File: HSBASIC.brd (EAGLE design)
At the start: 44 x 44 mm, 25 parts, among them IC1 ESP12SMT, IC3 MS563702BA03, IC4 DHT12

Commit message: Routing
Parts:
- removed R3: 10K, freetronics-jon:0603
- moved R10 1.50 mm to (26.0, 40.5), turned to 180 degrees
- moved R7 1.50 mm to (26.0, 40.5), turned to 0 degrees
- turned LED2 to 0 degrees
- turned LED3 to 180 degrees
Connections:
- removed net N$11: LED3.A, R7.1
- new net N$5: LED2.C, R10.2
- net 3.3V: now also LED2.A, LED3.A; no longer R3.2
- net GND: no longer LED2.C, LED3.C
- net GPIO16: no longer R10.2, R7.2
- net GPIO2: now also R10.1, R7.1; no longer R3.1
- net N$4: now also LED3.C, R7.2; no longer LED2.A, R10.1
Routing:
- net GPIO2: track 17.0 -> 33.8 mm, vias 0 -> 2
- net GPIO16: track 13.6 -> 0.00 mm, vias 1 -> 0
- net 3.3V: track 110.5 -> 123.5 mm, vias 2 -> 3
- net N$11: track 3.98 -> 0.00 mm
- net N$5: track 0.00 -> 2.48 mm
- net N$4: track 3.98 -> 2.48 mm
- net GND: track 27.9 -> 28.9 mm
- net TXD: track 45.0 -> 44.4 mm
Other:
- outline, holes or cut-outs redrawn

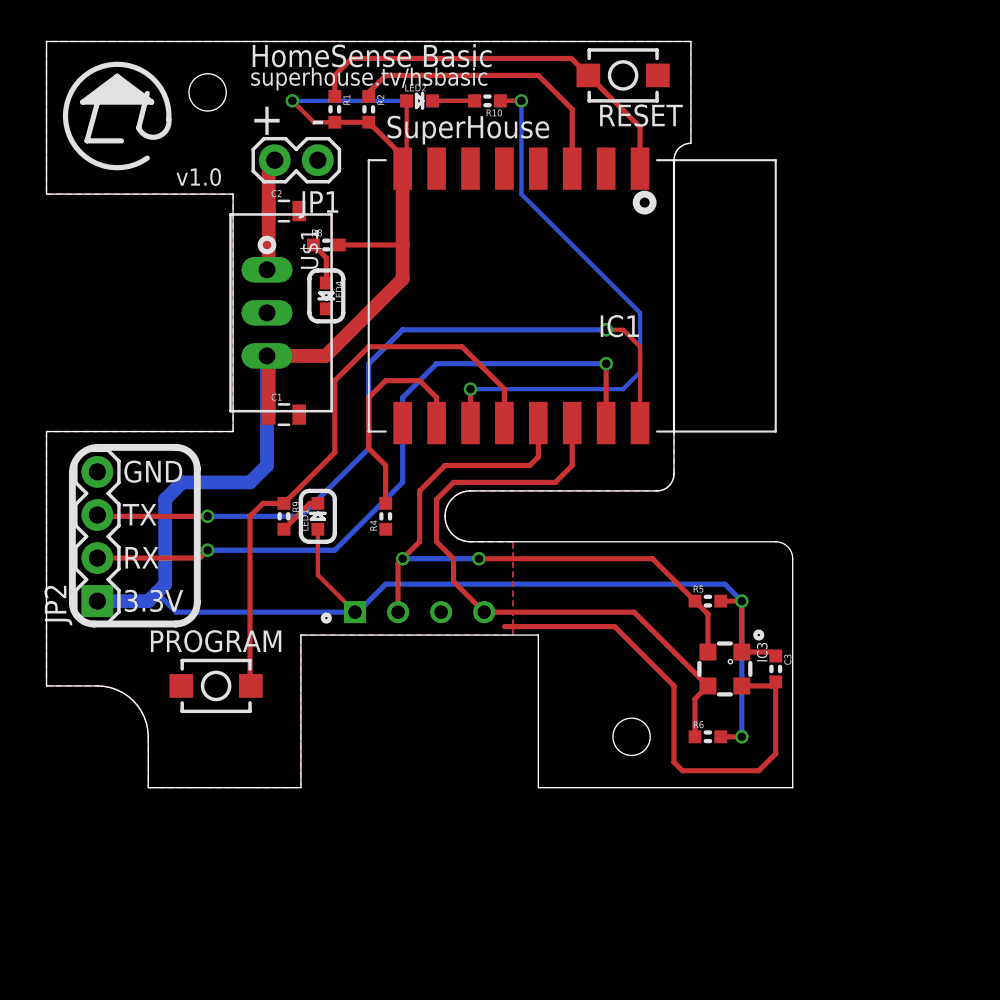
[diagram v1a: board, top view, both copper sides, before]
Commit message: Switch to BME280 sensor for Tasmota compatibility
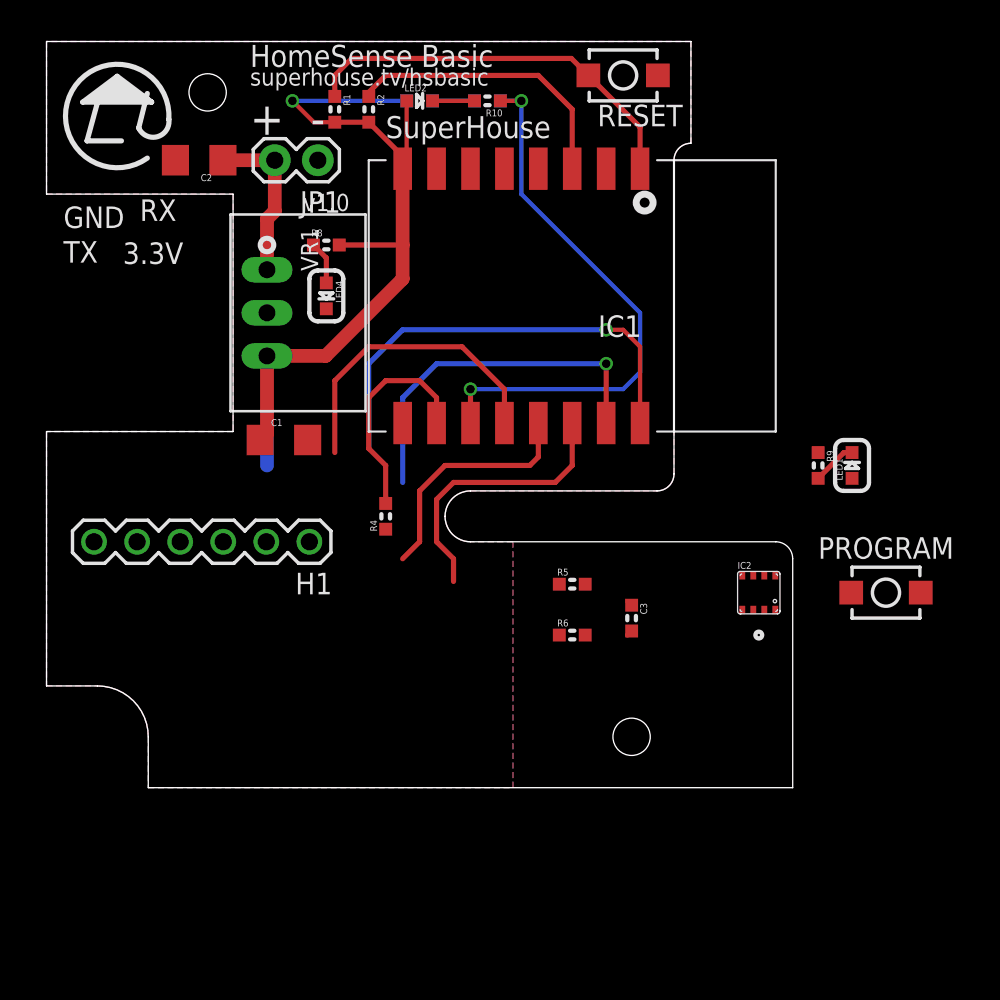
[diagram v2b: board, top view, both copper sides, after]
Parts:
- removed IC3: MS563702BA03, freetronics-jon:MS5637
- removed IC4: DHT12, freetronics-jon:DHT12
- removed JP2: (no value), freetronics-jon:1X04
- removed U$1: K7803-500R3, freetronics-jon:K78XX-500R3
- added H1: Program, SuperHouse-Connectors:1X06-S
- added IC2: BME280, SuperHouse-Sensors:BME280
- added VR1: K7803-500R3, SuperHouse-Regulators:K78XX-500R3
- C1, C2: device freetronics-jon:0805 -> SuperHouse-DiscreteSemi:C1206
- C3: device freetronics-jon:0603 -> SuperHouse-DiscreteSemi:C0603
- IC1: value ESP12SMT -> ESP12-SMT; device freetronics-jon:ESP12 -> SuperHouse-MCUs:ESP12
- LED1, LED2, LED3, LED4: device freetronics-jon:LED-0603 -> SuperHouse-LEDs:LED-0603
- R1, R10, R2, R4, R5, R6, R7, R8, R9: device freetronics-jon:0603 -> SuperHouse-DiscreteSemi:R0603
- S1, S2: device freetronics-jon:TACTILE_SWITCH_SMD_2PIN_TINY -> SuperHouse-Switches:TACTILE_SMD_3X4X2
- moved S2 39.9 mm to (49.5, 11.5)
- moved LED1 31.6 mm to (47.5, 19.0)
- moved R9 31.6 mm to (45.5, 19.0)
- moved R6 10.0 mm to (31.0, 9.00)
- moved C3 9.01 mm to (34.5, 10.0)
- moved R5 8.06 mm to (31.0, 12.0)
- moved C2 5.83 mm to (9.00, 37.0), turned to 180 degrees
- moved C1 1.50 mm to (14.0, 20.5)
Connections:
- net 3.3V: now also H1.6, IC2.2, IC2.6, IC2.8, VR1.3; no longer IC3.1, IC4.1, JP2.1, U$1.3
- net GND: now also H1.3, IC2.1, IC2.5, IC2.7, VR1.2; no longer IC3.4, IC4.3, JP2.4, U$1.2
- net GPIO0: now also H1.1
- net N$1: now also VR1.1; no longer U$1.1
- net RESET: now also H1.2
- net RXD: now also H1.5; no longer JP2.2
- net SCL: now also IC2.4; no longer IC3.3, IC4.4
- net SDA: now also IC2.3; no longer IC3.2, IC4.2
- net TXD: now also H1.4; no longer JP2.3
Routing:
- net 3.3V: track 123.5 -> 51.5 mm, vias 3 -> 1
- net GND: track 28.9 -> 0.34 mm
- net SDA: track 39.1 -> 14.2 mm, vias 2 -> 0
- net SCL: track 37.4 -> 16.6 mm
- net RXD: track 41.2 -> 21.3 mm, vias 2 -> 1
- net TXD: track 44.4 -> 26.7 mm, vias 2 -> 1
- net GPIO0: track 34.7 -> 18.2 mm
- net N$1: track 6.65 -> 9.71 mm
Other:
- outline, holes or cut-outs redrawn

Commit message: Routing progress
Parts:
- removed H1: Program, SuperHouse-Connectors:1X06-S
- added J1: ESPROG-SOCKET, SuperHouse-Connectors:ESPROG-S
- added J2: (no value), SuperHouse-Connectors:1X04
- moved LED1 44.0 mm to (3.50, 19.0), turned to 0 degrees
- moved S2 42.2 mm to (8.00, 19.0)
- moved R9 42.0 mm to (3.50, 17.2), turned to 180 degrees
- moved C3 16.6 mm to (19.0, 16.0), turned to 90 degrees
- moved R5 10.8 mm to (21.0, 16.0), turned to 270 degrees
- moved R6 9.82 mm to (33.5, 18.5)
- moved R4 3.00 mm to (17.0, 16.0)
- moved IC2 1.12 mm to (41.5, 12.5), turned to 270 degrees
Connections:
- removed net RESET: H1.2, IC1.1, R1.1, S1.1
- new net !RESET: IC1.1, J1.6, R1.1, S1.1
- net 3.3V: now also J1.3, J2.3; no longer H1.6
- net GND: now also J1.1, J2.4; no longer H1.3
- net GPIO0: now also J1.2; no longer H1.1
- net RXD: now also J1.4; no longer H1.5
- net SCL: now also J2.2
- net SDA: now also J2.1
- net TXD: now also J1.5; no longer H1.4
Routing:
- net !RESET: track 0.00 -> 62.2 mm, vias 0 -> 1
- net SCL: track 16.6 -> 50.7 mm
- net SDA: track 14.2 -> 46.2 mm
- net GND: track 0.34 -> 27.5 mm, vias 0 -> 2
- net RESET: track 23.8 -> 0.00 mm
- net GPIO0: track 18.2 -> 36.3 mm
- net TXD: track 26.7 -> 41.3 mm
- net RXD: track 21.3 -> 34.3 mm
- net 3.3V: track 51.5 -> 62.2 mm, vias 1 -> 5
- added copper zone on layer 16, net 3.3V
- removed copper zone on layer 16, net GND
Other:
- outline, holes or cut-outs redrawn
- board text added: "v2.0"
- board text removed: "v1.0"

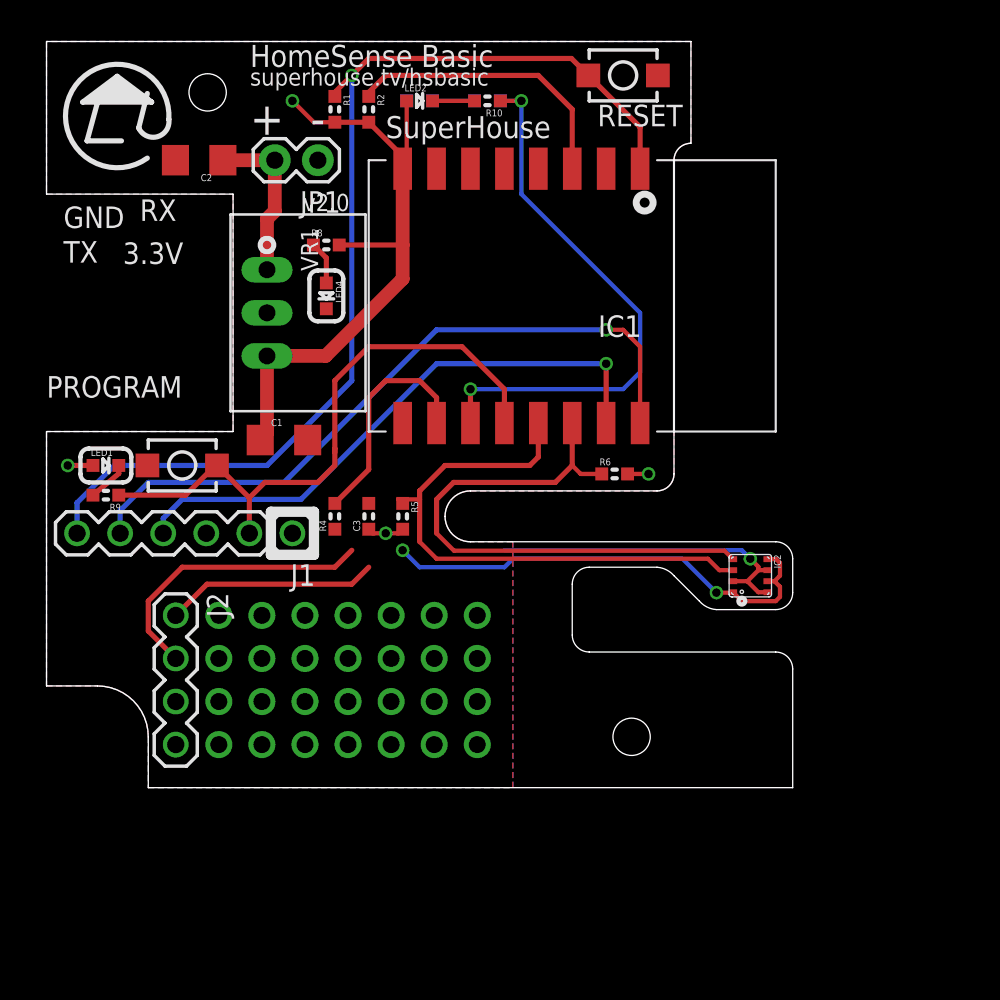
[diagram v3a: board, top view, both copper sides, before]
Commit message: Routing I2C
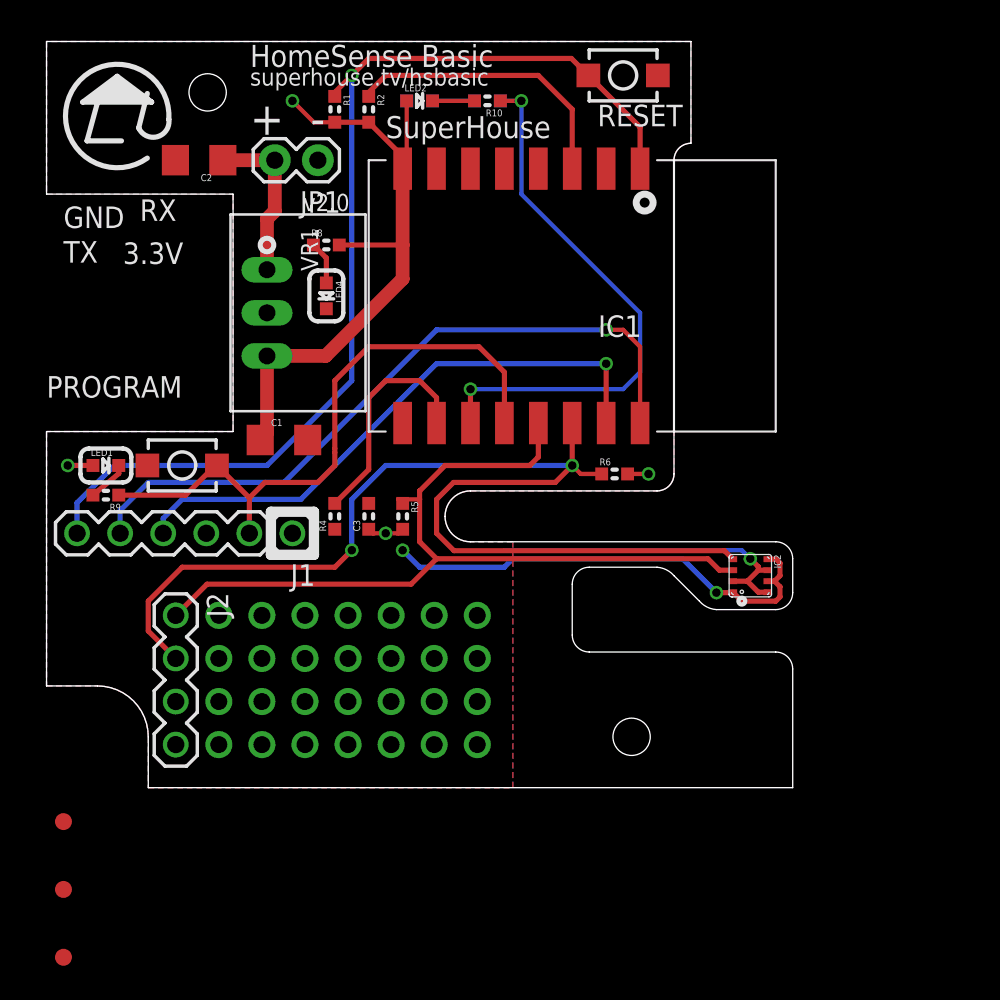
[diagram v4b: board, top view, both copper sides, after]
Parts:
- added FID1, FID2, FID3: FIDUCIAL1X2.5, freetronics:FIDUCIAL-1X2.5
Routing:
- net SCL: track 50.7 -> 67.5 mm, vias 0 -> 2
- net SDA: track 46.2 -> 50.4 mm
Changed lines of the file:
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@@
 </layers>
 <board>
-<fusionsync huburn="a.cGVyc29uYWw6dWUyZDliZmNi" projecturn="a.cGVyc29uYWw6dWUyZDliZmNiIzIwMTkwNjE5MTk5NjgzNjgx" f3durn="urn:adsk.wipprod:dm.lineage:OGjb5C-sRfSX_GoFxLdnUw" pcbguid="54a2e106-a76a-4605-8f7a-9ec732ccbce4" lastpulledtime="" lastsyncedchangeguid="4bc554cd-7b2e-ae2c-27ba-0ab9a2369358"/>
+<fusionsync huburn="a.cGVyc29uYWw6dWUyZDliZmNi" projecturn="a.cGVyc29uYWw6dWUyZDliZmNiIzIwMTkwNjE5MTk5NjgzNjgx" f3durn="urn:adsk.wipprod:dm.lineage:OGjb5C-sRfSX_GoFxLdnUw" pcbguid="54a2e106-a76a-4605-8f7a-9ec732ccbce4" lastpulledtime="" lastsyncedchangeguid="327c1767-6b57-4ca5-d82e-19adec99c66e"/>
 <plain>
 <wire x1="0" y1="6" x2="0" y2="21" width="0.0254" layer="20"/>
@@
 <attribute name="VALUE" x="4.445" y="11.43" size="1.27" layer="27" rot="R270"/>
 </element>
+<element name="FID1" library="freetronics" package="FIDUCIAL-1X2.5" value="FIDUCIAL1X2.5" x="1" y="-2" smashed="yes"/>
+<element name="FID2" library="freetronics" package="FIDUCIAL-1X2.5" value="FIDUCIAL1X2.5" x="1" y="-6" smashed="yes"/>
+<element name="FID3" library="freetronics" package="FIDUCIAL-1X2.5" value="FIDUCIAL1X2.5" x="1" y="-10" smashed="yes"/>
 </elements>
 <signals>
@@
 <contactref element="IC2" pad="5"/>
 <contactref element="J1" pad="1"/>
-<wire x1="42.525" y1="12.175" x2="42.925" y2="12.175" width="0.254" layer="1"/>
-<wire x1="43.25" y1="12.5" x2="42.925" y2="12.175" width="0.254" layer="1"/>
-<wire x1="42.525" y1="13.475" x2="43.025" y2="13.475" width="0.254" layer="1"/>
-<wire x1="43.025" y1="13.475" x2="43.25" y2="13.25" width="0.254" layer="1"/>
-<wire x1="43.25" y1="13.25" x2="43.25" y2="12.5" width="0.254" layer="1"/>
-<wire x1="40.475" y1="11.525" x2="41" y2="11" width="0.254" layer="1"/>
-<wire x1="43" y1="11" x2="43.25" y2="11.25" width="0.254" layer="1"/>
-<wire x1="43.25" y1="11.25" x2="43.25" y2="11.85" width="0.254" layer="1"/>
-<wire x1="43.25" y1="11.85" x2="42.925" y2="12.175" width="0.254" layer="1"/>
-<wire x1="41" y1="11" x2="43" y2="11" width="0.254" layer="1"/>
+<wire x1="42.525" y1="12.175" x2="42.925" y2="12.175" width="0.3048" layer="1"/>
+<wire x1="43.25" y1="12.5" x2="42.925" y2="12.175" width="0.3048" layer="1"/>
+<wire x1="42.525" y1="13.475" x2="43.025" y2="13.475" width="0.3048" layer="1"/>
+<wire x1="43.025" y1="13.475" x2="43.25" y2="13.25" width="0.3048" layer="1"/>
+<wire x1="43.25" y1="13.25" x2="43.25" y2="12.5" width="0.3048" layer="1"/>
+<wire x1="40.475" y1="11.525" x2="41" y2="11" width="0.3048" layer="1"/>
+<wire x1="43" y1="11" x2="43.25" y2="11.25" width="0.3048" layer="1"/>
+<wire x1="43.25" y1="11.25" x2="43.25" y2="11.85" width="0.3048" layer="1"/>
+<wire x1="43.25" y1="11.85" x2="42.925" y2="12.175" width="0.3048" layer="1"/>
+<wire x1="41" y1="11" x2="43" y2="11" width="0.3048" layer="1"/>
 <via x="39.5" y="11.5" extent="1-16" drill="0.5"/>
 <wire x1="40.475" y1="11.525" x2="40.45" y2="11.5" width="0.254" layer="1"/>
-<wire x1="40.45" y1="11.5" x2="39.5" y2="11.5" width="0.254" layer="1"/>
-<wire x1="39.5" y1="11.5" x2="37.5" y2="13.5" width="0.254" layer="16"/>
-<wire x1="27.5" y1="13.5" x2="27" y2="13" width="0.254" layer="16"/>
-<wire x1="27" y1="13" x2="22" y2="13" width="0.254" layer="16"/>
-<wire x1="22" y1="13" x2="21" y2="14" width="0.254" layer="16"/>
-<wire x1="37.5" y1="13.5" x2="27.5" y2="13.5" width="0.254" layer="16"/>
+<wire x1="40.45" y1="11.5" x2="39.5" y2="11.5" width="0.3048" layer="1"/>
+<wire x1="39.5" y1="11.5" x2="37.5" y2="13.5" width="0.3048" layer="16"/>
+<wire x1="27.5" y1="13.5" x2="27" y2="13" width="0.3048" layer="16"/>
+<wire x1="27" y1="13" x2="22" y2="13" width="0.3048" layer="16"/>
+<wire x1="22" y1="13" x2="21" y2="14" width="0.3048" layer="16"/>
+<wire x1="37.5" y1="13.5" x2="27.5" y2="13.5" width="0.3048" layer="16"/>
 <via x="21" y="14" extent="1-16" drill="0.5"/>
 <contactref element="J2" pad="4"/>
@@
 <wire x1="23.5" y1="19" x2="28.5" y2="19" width="0.3048" layer="1"/>
 <contactref element="IC2" pad="3"/>
-<wire x1="39.675" y1="12.825" x2="39" y2="13.5" width="0.254" layer="1"/>
-<wire x1="40.475" y1="12.825" x2="39.675" y2="12.825" width="0.254" layer="1"/>
-<wire x1="23" y1="13.5" x2="22" y2="14.5" width="0.254" layer="1"/>
-<wire x1="39" y1="13.5" x2="23" y2="13.5" width="0.254" layer="1"/>
+<wire x1="39.675" y1="12.825" x2="39" y2="13.5" width="0.3048" layer="1"/>
+<wire x1="40.475" y1="12.825" x2="39.675" y2="12.825" width="0.3048" layer="1"/>
+<wire x1="23" y1="13.5" x2="22" y2="14.5" width="0.3048" layer="1"/>
+<wire x1="39" y1="13.5" x2="23" y2="13.5" width="0.3048" layer="1"/>
 <wire x1="21" y1="16.762" x2="20.738" y2="17" width="0.254" layer="1"/>
 <wire x1="20.738" y1="17" x2="22" y2="17" width="0.254" layer="1"/>
 <contactref element="J2" pad="1"/>
 <wire x1="7.62" y1="10.16" x2="9.46" y2="12" width="0.3048" layer="1"/>
-<wire x1="18" y1="12" x2="19" y2="13" width="0.3048" layer="1"/>
-<wire x1="9.46" y1="12" x2="18" y2="12" width="0.3048" layer="1"/>
-<wire x1="19" y1="13" x2="21" y2="16.762" width="0" layer="19" extent="1-1"/>
+<wire x1="21.5" y1="12" x2="23" y2="13.5" width="0.3048" layer="1"/>
+<wire x1="9.46" y1="12" x2="21.5" y2="12" width="0.3048" layer="1"/>
 </signal>
 <signal name="SCL">
@@
 <wire x1="31" y1="19" x2="31" y2="21.5" width="0.3048" layer="1"/>
 <contactref element="IC2" pad="4"/>
-<wire x1="40.475" y1="13.475" x2="39.975" y2="13.975" width="0.254" layer="1"/>
+<wire x1="40.475" y1="13.475" x2="39.975" y2="13.975" width="0.3048" layer="1"/>
 <wire x1="32.738" y1="18.5" x2="31.5" y2="18.5" width="0.254" layer="1"/>
 <wire x1="31.5" y1="18.5" x2="31" y2="19" width="0.254" layer="1"/>
-<wire x1="24.025" y1="13.975" x2="23" y2="15" width="0.254" layer="1"/>
-<wire x1="39.975" y1="13.975" x2="24.025" y2="13.975" width="0.254" layer="1"/>
+<wire x1="24.025" y1="13.975" x2="23" y2="15" width="0.3048" layer="1"/>
+<wire x1="39.975" y1="13.975" x2="24.025" y2="13.975" width="0.3048" layer="1"/>
 <contactref element="J2" pad="2"/>
 <wire x1="7.62" y1="7.62" x2="6" y2="9.24" width="0.3048" layer="1"/>
@@
 <wire x1="8" y1="13" x2="17" y2="13" width="0.3048" layer="1"/>
 <wire x1="17" y1="13" x2="18" y2="14" width="0.3048" layer="1"/>
-<wire x1="18" y1="14" x2="31" y2="21.5" width="0" layer="19" extent="1-1"/>
+<via x="18" y="14" extent="1-16" drill="0.5"/>
+<wire x1="18" y1="17" x2="20" y2="19" width="0.3048" layer="16"/>
+<wire x1="18" y1="14" x2="18" y2="17" width="0.3048" layer="16"/>
+<via x="31" y="19" extent="1-16" drill="0.5"/>
+<wire x1="20" y1="19" x2="31" y2="19" width="0.3048" layer="16"/>
 </signal>
 <signal name="GPIO0">
 <contactref element="IC1" pad="12"/>
 <contactref element="R9" pad="1"/>
-<wire x1="19" y1="26" x2="24.5" y2="26" width="0.3048" layer="1"/>
-<wire x1="24.5" y1="26" x2="27" y2="23.5" width="0.3048" layer="1"/>
-<wire x1="27" y1="23.5" x2="27" y2="21.5" width="0.3048" layer="1"/>
+<wire x1="19" y1="26" x2="25.5" y2="26" width="0.3048" layer="1"/>
+<wire x1="25.5" y1="26" x2="27" y2="24.5" width="0.3048" layer="1"/>
+<wire x1="27" y1="24.5" x2="27" y2="21.5" width="0.3048" layer="1"/>
 <contactref element="S2" pad="2"/>
 <wire x1="17" y1="19.762" x2="17" y2="20" width="0.3048" layer="1"/>
@@
 <wire x1="11.96" y1="15" x2="11.96" y2="17.09" width="0.3048" layer="1"/>
 <wire x1="11.96" y1="17.09" x2="10.05" y2="19" width="0.3048" layer="1"/>
-<wire x1="17" y1="20" x2="17" y2="19" width="0.3048" layer="1"/>
+<wire x1="17" y1="19.762" x2="17" y2="19" width="0.3048" layer="1"/>
 <wire x1="17" y1="19" x2="16" y2="18" width="0.3048" layer="1"/>
 <wire x1="12.87" y1="18" x2="11.96" y2="17.09" width="0.3048" layer="1"/>
@@
 <vertex x="38" y="38"/>
 </polygon>
-<wire x1="42.525" y1="11.525" x2="41.975" y2="11.525" width="0.254" layer="1"/>
-<wire x1="40.475" y1="12.175" x2="41.325" y2="12.175" width="0.254" layer="1"/>
-<wire x1="41.975" y1="11.525" x2="41.325" y2="12.175" width="0.254" layer="1"/>
-<wire x1="42.525" y1="12.825" x2="41.975" y2="12.825" width="0.254" layer="1"/>
-<wire x1="41.325" y1="12.175" x2="41.975" y2="12.825" width="0.254" layer="1"/>
+<wire x1="42.525" y1="11.525" x2="41.975" y2="11.525" width="0.3048" layer="1"/>
+<wire x1="40.475" y1="12.175" x2="41.325" y2="12.175" width="0.3048" layer="1"/>
+<wire x1="41.975" y1="11.525" x2="41.325" y2="12.175" width="0.3048" layer="1"/>
+<wire x1="42.525" y1="12.825" x2="41.975" y2="12.825" width="0.3048" layer="1"/>
+<wire x1="41.325" y1="12.175" x2="41.975" y2="12.825" width="0.3048" layer="1"/>
 <via x="41.5" y="13.5" extent="1-16" drill="0.5"/>
-<wire x1="41.975" y1="12.825" x2="41.975" y2="13.025" width="0.254" layer="1"/>
-<wire x1="41.975" y1="13.025" x2="41.5" y2="13.5" width="0.254" layer="1"/>
+<wire x1="41.975" y1="12.825" x2="41.975" y2="13.025" width="0.3048" layer="1"/>
+<wire x1="41.975" y1="13.025" x2="41.5" y2="13.5" width="0.3048" layer="1"/>
 <via x="35.5" y="18.5" extent="1-16" drill="0.5"/>
 <wire x1="34.262" y1="18.5" x2="35.5" y2="18.5" width="0.254" layer="1"/>

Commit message: Hopefully final routing for v2.0 release
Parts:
- removed FID1: FIDUCIAL1X2.5, freetronics:FIDUCIAL-1X2.5
- C1, C2: device SuperHouse-DiscreteSemi:C1206 -> SuperHouse-DiscreteSemi:C0805
- J2: value (none) -> I2C
- JP1: value (none) -> PWR
- S1, S2: device SuperHouse-Switches:TACTILE_SMD_3X4X2 -> SuperHouse-Switches:TACTILE_SMT_3X4X2
- VR1: device SuperHouse-Regulators:K78XX-500R3 -> SuperHouse-Regulators:K78XX-500R3-FLAT
- moved FID3 52.8 mm to (33.0, 32.0)
- moved FID2 14.0 mm to (2.00, 8.00)
- moved C2 5.83 mm to (14.0, 34.0), turned to 0 degrees
- moved C1 1.50 mm to (14.0, 22.0)
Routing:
- net N$1: track 9.71 -> 6.65 mm
- net 3.3V: track 62.2 -> 60.6 mm
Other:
- board text added: "!RST"
- board text added: "3.3"
- board text added: "5- 24V"
- board text added: "ESProg"
- board text added: "FLASH"
- board text added: "IO0"
- board text added: "RXi"
- board text added: "SCL"
- board text added: "SDA"
- board text added: "Super House"
- board text added: "TXo"
- board text added: "by Jon Oxer"
- board text removed: "3.3V"
- board text removed: "PROGRAM"
- board text removed: "RX"
- board text removed: "SuperHouse"
- board text removed: "TX"
